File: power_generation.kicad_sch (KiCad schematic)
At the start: 35 parts, among them J301 61300211121, J302 61300211121, J303 EMI shield frame, U301 AP64500SP-13, U302 AP64500SP-13

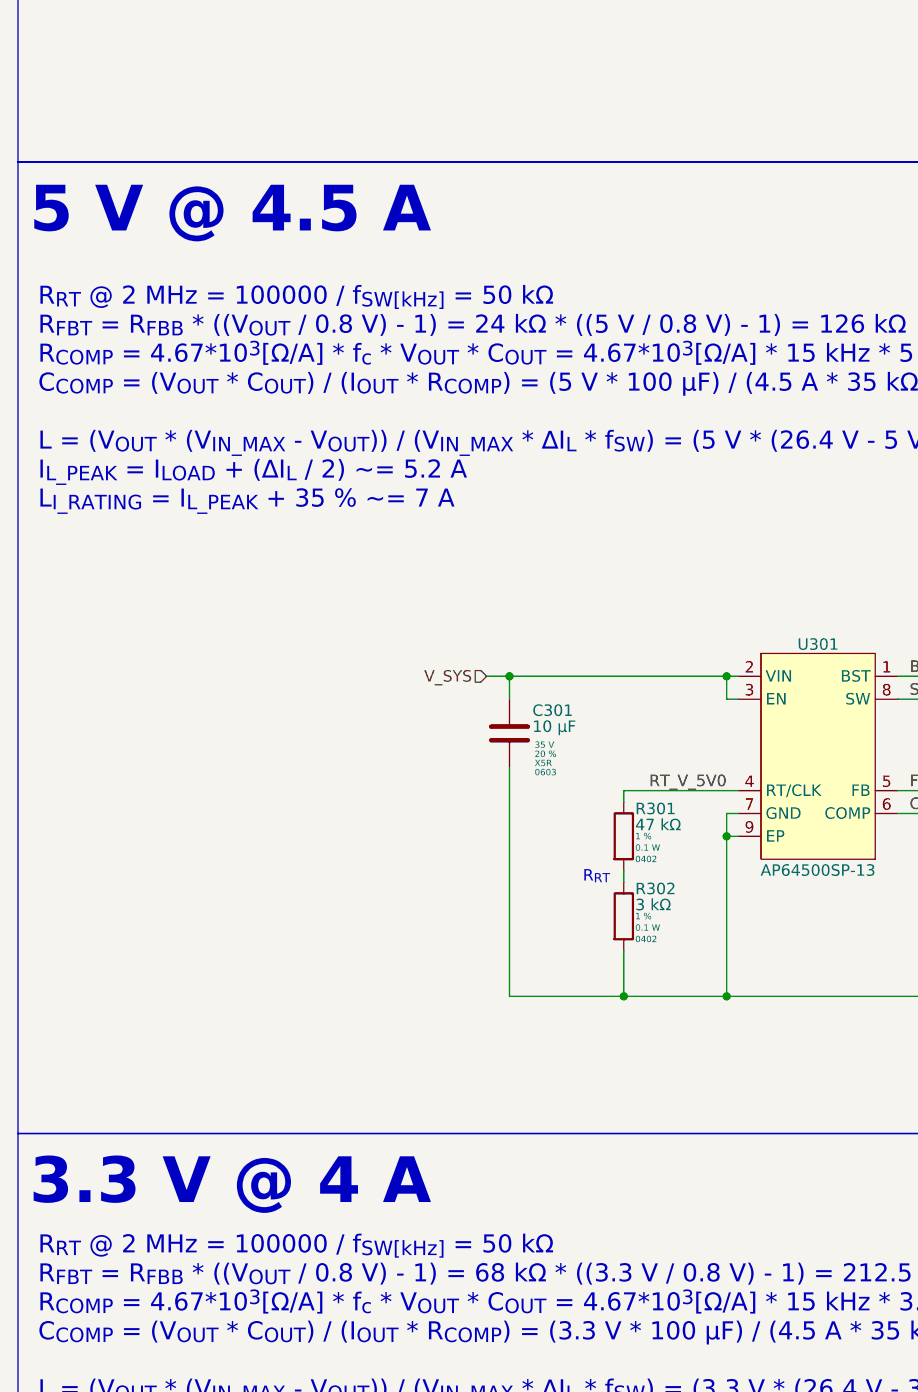
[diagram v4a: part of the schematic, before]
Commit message: Fix power connections
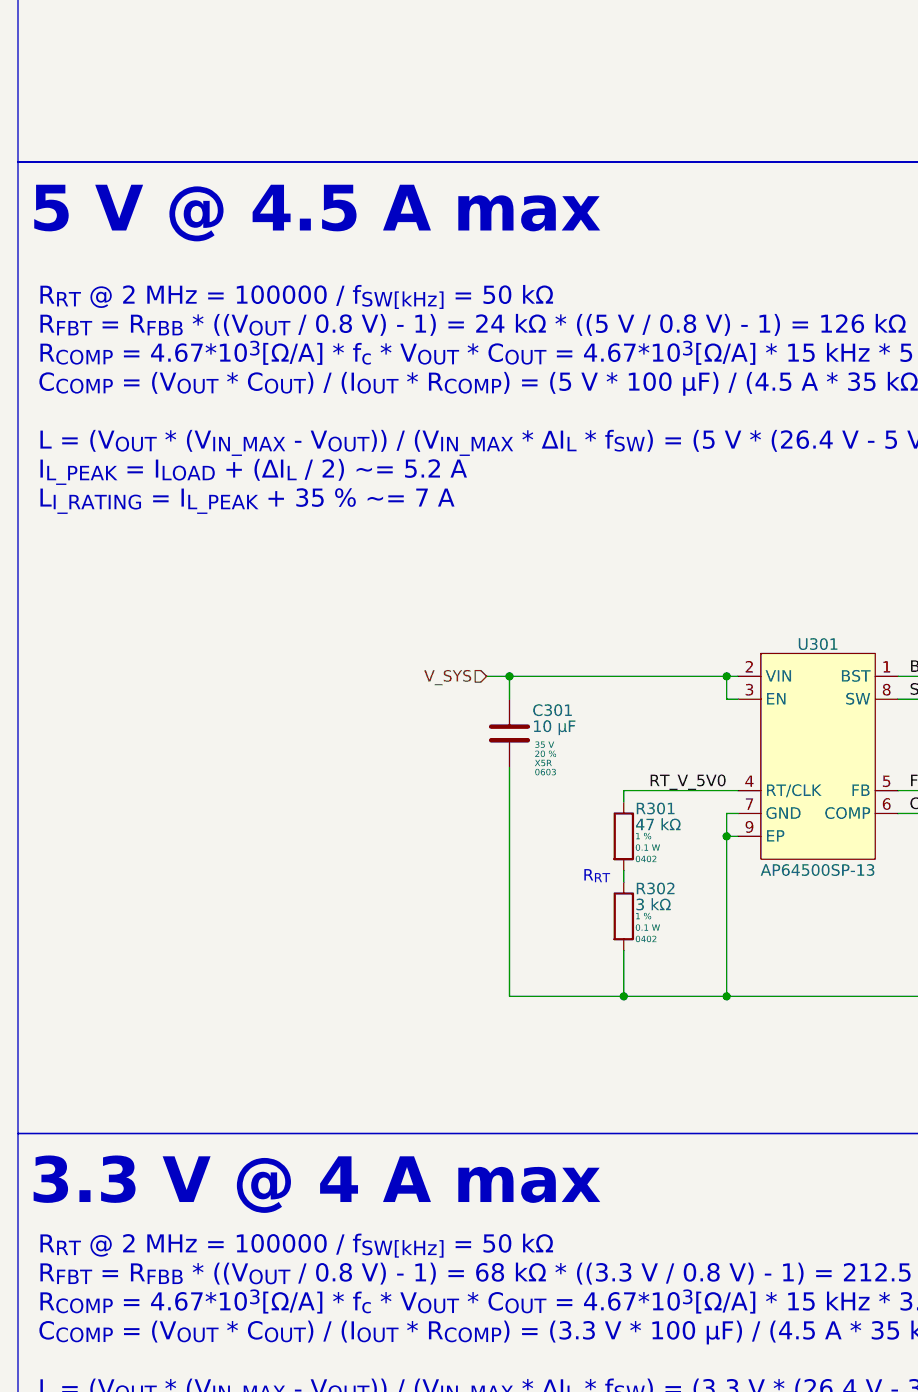
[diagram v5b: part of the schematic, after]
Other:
- note added: "3.3 V @ 4 A max"
- note added: "5 V @ 4.5 A max"
- note removed: "3.3 V @ 4 A"
- note removed: "5 V @ 4.5 A"
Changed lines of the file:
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@@
 		)
 	)
-	(text "3.3 V @ 4 A"
+	(text "3.3 V @ 4 A max"
 		(exclude_from_sim no)
 		(at 13.97 148.59 0)
@@
 		)
 	)
-	(text "5 V @ 4.5 A"
+	(text "5 V @ 4.5 A max"
 		(exclude_from_sim no)
 		(at 13.97 40.64 0)

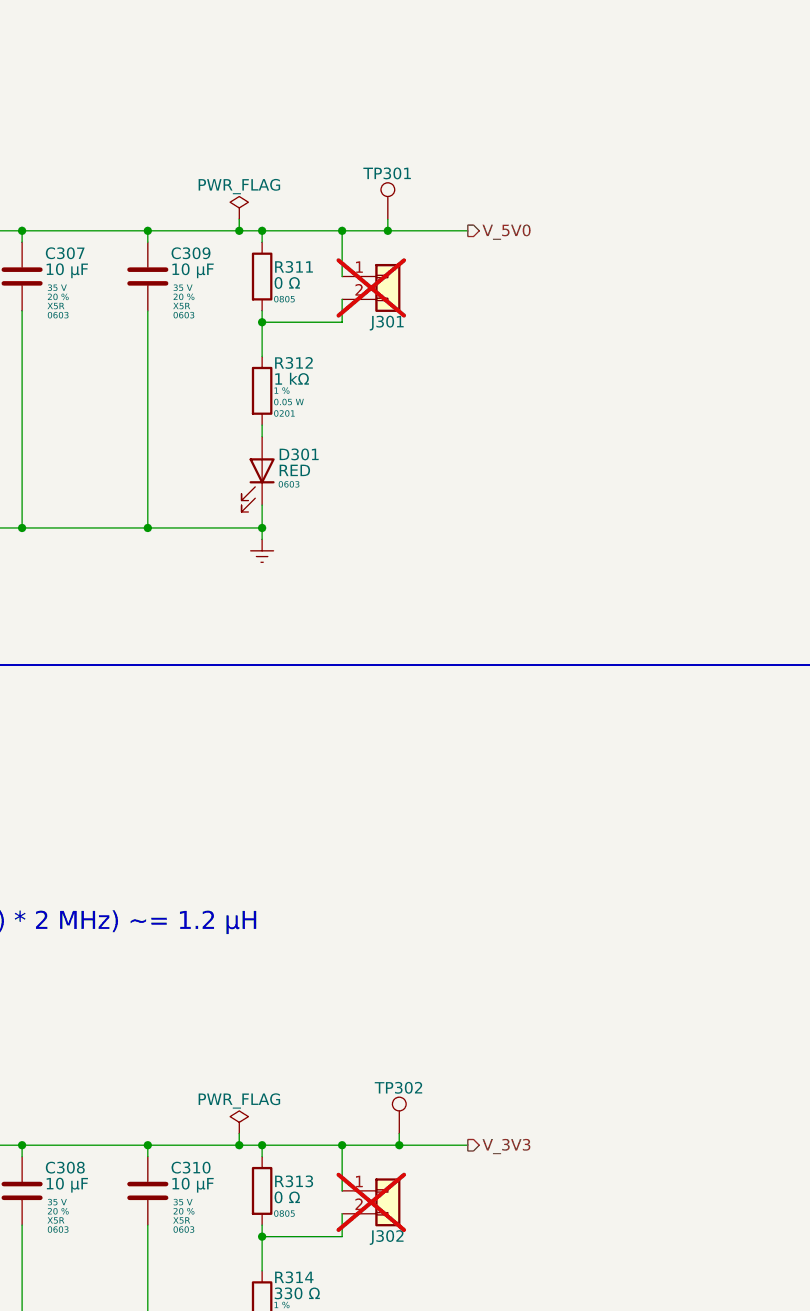
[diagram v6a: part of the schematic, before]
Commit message: Remove redundant test points, fix layouts
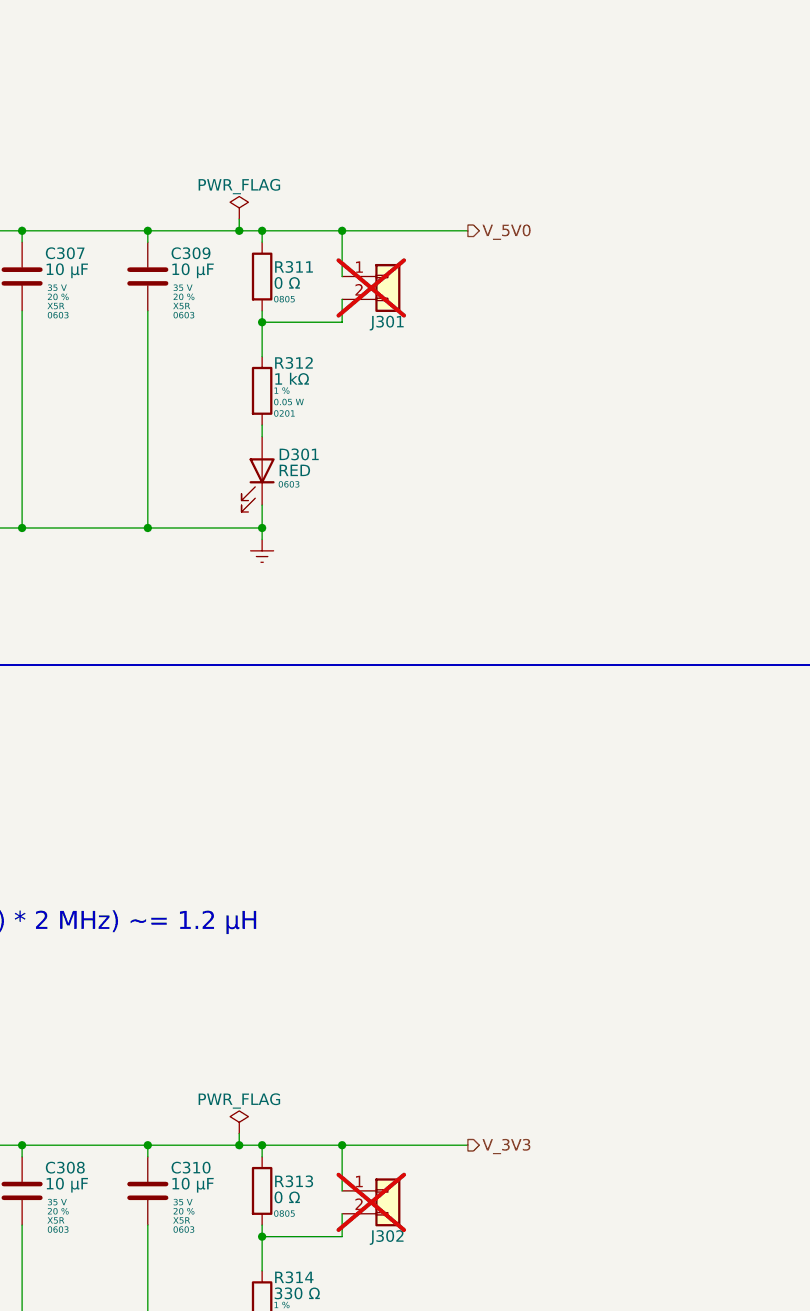
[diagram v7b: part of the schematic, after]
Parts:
- removed TP301, TP302: TestPoint, TestPoint:TestPoint_Pad_D1.0mm, symbol Connector:TestPoint
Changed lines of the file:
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@@
 	)
 	(junction
-		(at 196.85 199.39)
-		(diameter 0)
-		(color 0 0 0 0)
-	)
-	(junction
 		(at 181.61 199.39)
 		(diameter 0)
@@
 		(color 0 0 0 0)
 	)
-	(junction
-		(at 195.58 97.79)
-		(diameter 0)
-		(color 0 0 0 0)
-	)
 	(wire
 		(pts
@@
 	(wire
 		(pts
-			(xy 195.58 96.52) (xy 195.58 97.79)
-		)
-		(stroke
-			(width 0)
-			(type default)
-		)
-	)
-	(wire
-		(pts
 			(xy 168.91 130.81) (xy 181.61 130.81)
 		)
@@
 	(wire
 		(pts
-			(xy 196.85 198.12) (xy 196.85 199.39)
-		)
-		(stroke
-			(width 0)
-			(type default)
-		)
-	)
-	(wire
-		(pts
-			(xy 196.85 199.39) (xy 204.47 199.39)
+			(xy 190.5 199.39) (xy 204.47 199.39)
 		)
 		(stroke
@@
 	(wire
 		(pts
-			(xy 190.5 97.79) (xy 195.58 97.79)
-		)
-		(stroke
-			(width 0)
-			(type default)
-		)
-	)
-	(wire
-		(pts
 			(xy 80.01 125.73) (xy 80.01 130.81)
 		)
@@
 	(wire
 		(pts
-			(xy 195.58 97.79) (xy 204.47 97.79)
+			(xy 190.5 97.79) (xy 204.47 97.79)
 		)
 		(stroke
@@
 	(wire
 		(pts
-			(xy 190.5 199.39) (xy 196.85 199.39)
-		)
-		(stroke
-			(width 0)
-			(type default)
-		)
-	)
-	(wire
-		(pts
 			(xy 154.94 199.39) (xy 154.94 200.66)
 		)
@@
 	)
 	(symbol
-		(lib_id "Connector:TestPoint")
-		(at 195.58 96.52 0)
-		(unit 1)
-		(exclude_from_sim no)
-		(in_bom yes)
-		(on_board yes)
-		(dnp no)
-		(property "Reference" "TP301"
-			(at 195.58 92.202 0)
-			(effects
-				(font
-					(size 1.27 1.27)
-				)
-				(justify bottom)
-			)
-		)
-		(property "Value" "TestPoint"
-			(at 198.12 93.218 90)
-			(effects
-				(font
-					(size 1.27 1.27)
-				)
-				(hide yes)
-			)
-		)
-		(property "Footprint" "TestPoint:TestPoint_Pad_D1.0mm"
-			(at 200.66 96.52 0)
-			(effects
-				(font
-					(size 1.27 1.27)
-				)
-				(hide yes)
-			)
-		)
-		(property "Datasheet" "~"
-			(at 200.66 96.52 0)
-			(effects
-				(font
-					(size 1.27 1.27)
-				)
-				(hide yes)
-			)
-		)
-		(property "Description" "test point"
-			(at 195.58 96.52 0)
-			(effects
-				(font
-					(size 1.27 1.27)
-				)
-				(hide yes)
-			)
-		)
-		(pin "1"
-		)
-		(instances
-			(project "linux-sbc"
-				(path "/fa11a02f-8043-4153-ab69-88d766503017/707b7ecb-79e2-4dd5-ae9a-df7ce3b9c75b"
-					(reference "TP301")
-					(unit 1)
-				)
-			)
-		)
-	)
-	(symbol
 		(lib_id "Device:C")
 		(at 168.91 102.87 0)
@@
 					(unit 1)
 				)
-			)
-		)
-	)
-	(symbol
-		(lib_id "Connector:TestPoint")
-		(at 196.85 198.12 0)
-		(unit 1)
-		(exclude_from_sim no)
-		(in_bom yes)
-		(on_board yes)
-		(dnp no)
-		(property "Reference" "TP302"
-			(at 196.85 193.802 0)
-			(effects
-				(font
-					(size 1.27 1.27)
-				)
-				(justify bottom)
-			)
-		)
-		(property "Value" "TestPoint"
-			(at 199.39 194.818 90)
-			(effects
-				(font
-					(size 1.27 1.27)
-				)
-				(hide yes)
-			)
-		)
-		(property "Footprint" "TestPoint:TestPoint_Pad_D1.0mm"
-			(at 201.93 198.12 0)
-			(effects
-				(font
-					(size 1.27 1.27)
-				)
-				(hide yes)
-			)
-		)
-		(property "Datasheet" "~"
-			(at 201.93 198.12 0)
-			(effects
-				(font
-					(size 1.27 1.27)
-				)
-				(hide yes)
-			)
-		)
-		(property "Description" "test point"
-			(at 196.85 198.12 0)
-			(effects
-				(font
-					(size 1.27 1.27)
-				)
-				(hide yes)
-			)
-		)
-		(pin "1"
-		)
-		(instances
-			(project "linux-sbc"
-				(path "/fa11a02f-8043-4153-ab69-88d766503017/707b7ecb-79e2-4dd5-ae9a-df7ce3b9c75b"
-					(reference "TP302")
-					(unit 1)
-				)

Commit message: Update 0402 footprints
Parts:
- C304, C306: footprint perfect_footprints:C_0402_1005Metric -> perfect_footprints:C_0402_1005Metric_HDI
- R301, R302, R303, R304: footprint perfect_footprints:R_0402_1005Metric -> perfect_footprints:R_0402_1005Metric_HDI
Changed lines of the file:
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@@
 			)
 		)
-		(property "Footprint" "perfect_footprints:R_0402_1005Metric"
+		(property "Footprint" "perfect_footprints:R_0402_1005Metric_HDI"
 			(at 78.232 223.52 90)
 			(effects
@@
 			)
 		)
-		(property "Footprint" "perfect_footprints:R_0402_1005Metric"
+		(property "Footprint" "perfect_footprints:R_0402_1005Metric_HDI"
 			(at 78.232 214.63 90)
 			(effects
@@
 			)
 		)
-		(property "Footprint" "perfect_footprints:R_0402_1005Metric"
+		(property "Footprint" "perfect_footprints:R_0402_1005Metric_HDI"
 			(at 78.232 113.03 90)
 			(effects
@@
 			)
 		)
-		(property "Footprint" "perfect_footprints:C_0402_1005Metric"
+		(property "Footprint" "perfect_footprints:C_0402_1005Metric_HDI"
 			(at 127.9652 128.27 0)
 			(effects
@@
 			)
 		)
-		(property "Footprint" "perfect_footprints:R_0402_1005Metric"
+		(property "Footprint" "perfect_footprints:R_0402_1005Metric_HDI"
 			(at 78.232 121.92 90)
 			(effects
@@
 			)
 		)
-		(property "Footprint" "perfect_footprints:C_0402_1005Metric"
+		(property "Footprint" "perfect_footprints:C_0402_1005Metric_HDI"
 			(at 127.9652 229.87 0)
 			(effects
